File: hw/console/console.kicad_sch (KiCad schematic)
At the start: 1 part, among them U1 F133-A

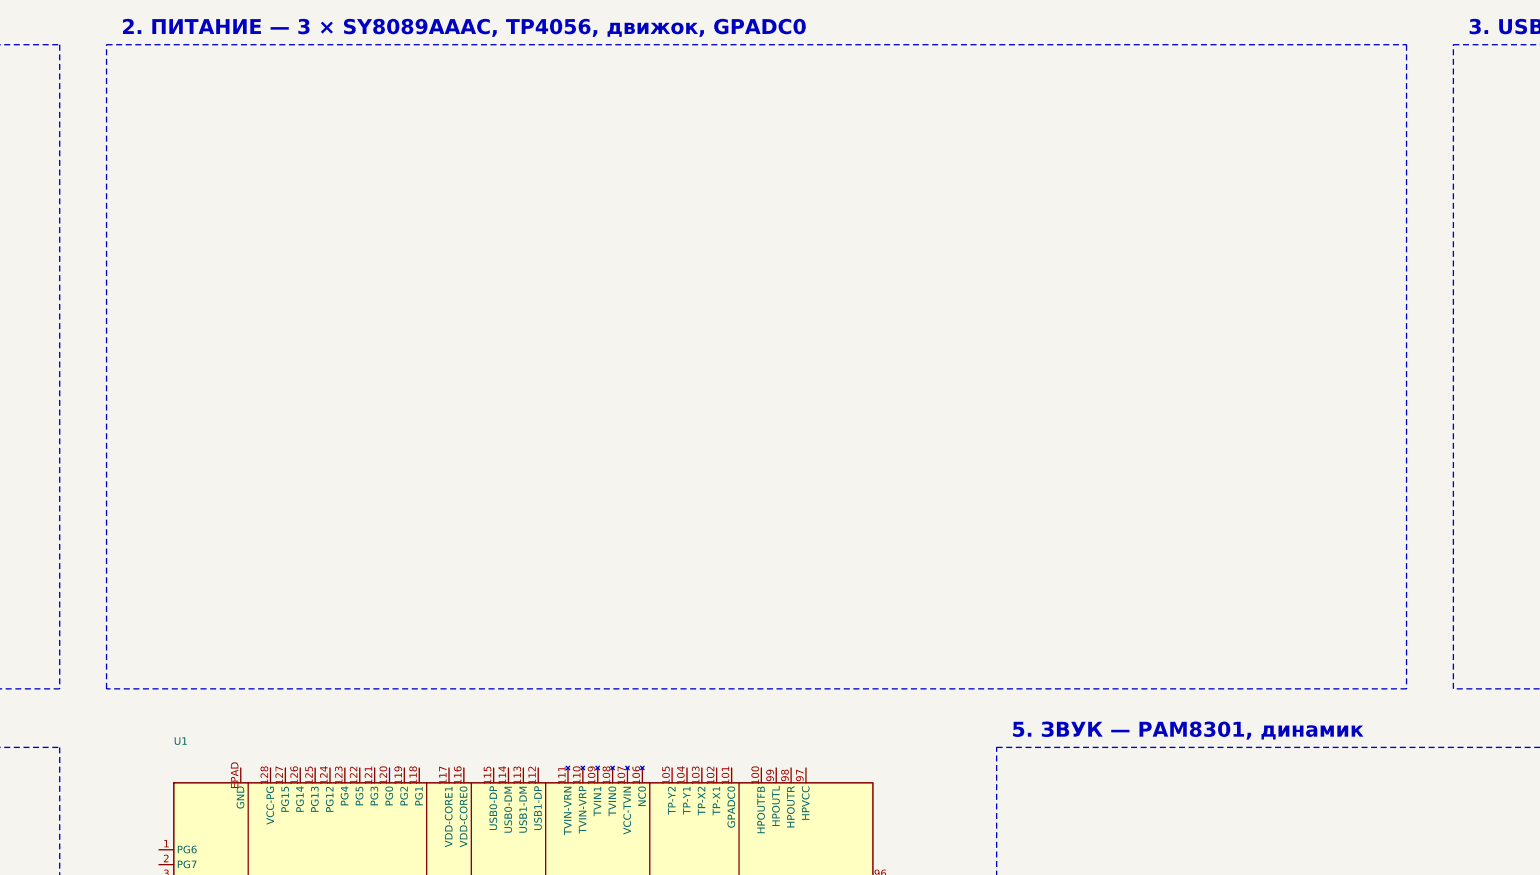
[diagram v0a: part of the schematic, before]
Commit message: hw: блок 2 «Питание» нарисован в KiCad
Три бака SY8089AAAC (3.3 / 1.8 / 0.9 В) с делителями MangoPi, RC-секвенсор
от движка, TP4056 с индикаторами, делитель банки на GPADC0, перемычки и
контрольные точки. Разъём банки — как J3 на плате v1.

Схема генерируется tools/block02_power.py: скрипт идемпотентный, у каждой
детали в поле «Источник» лежит раздел blocks/02-power.md — правило «ни одного
номинала без ссылки на источник» проверяется прямо по схеме.

Сверено по первоисточникам: распиновка SY8089 и TP4056 — по даташитам,
номиналы делителей и порядок старта рельс — по MangoPi. Netlist выгружен и
разобран по цепям: обратные связи, узел PWR_EN, VSYS, VBUS, GND и GPADC0
собираются целиком. ERC — 160 нарушений, все на невыведенных пока выводах
F133, кроме VBUS: его источник появится в блоке 3 вместе с разъёмом USB-C.

Отдельно: KiCad 9.0.9 не применяет (hide yes) в (effects), если рядом нет
(justify), — из-за этого служебные ссылки #PWR/#FLG печатались в PDF.

Co-Authored-By: Claude Opus 5 <noreply@anthropic.com>
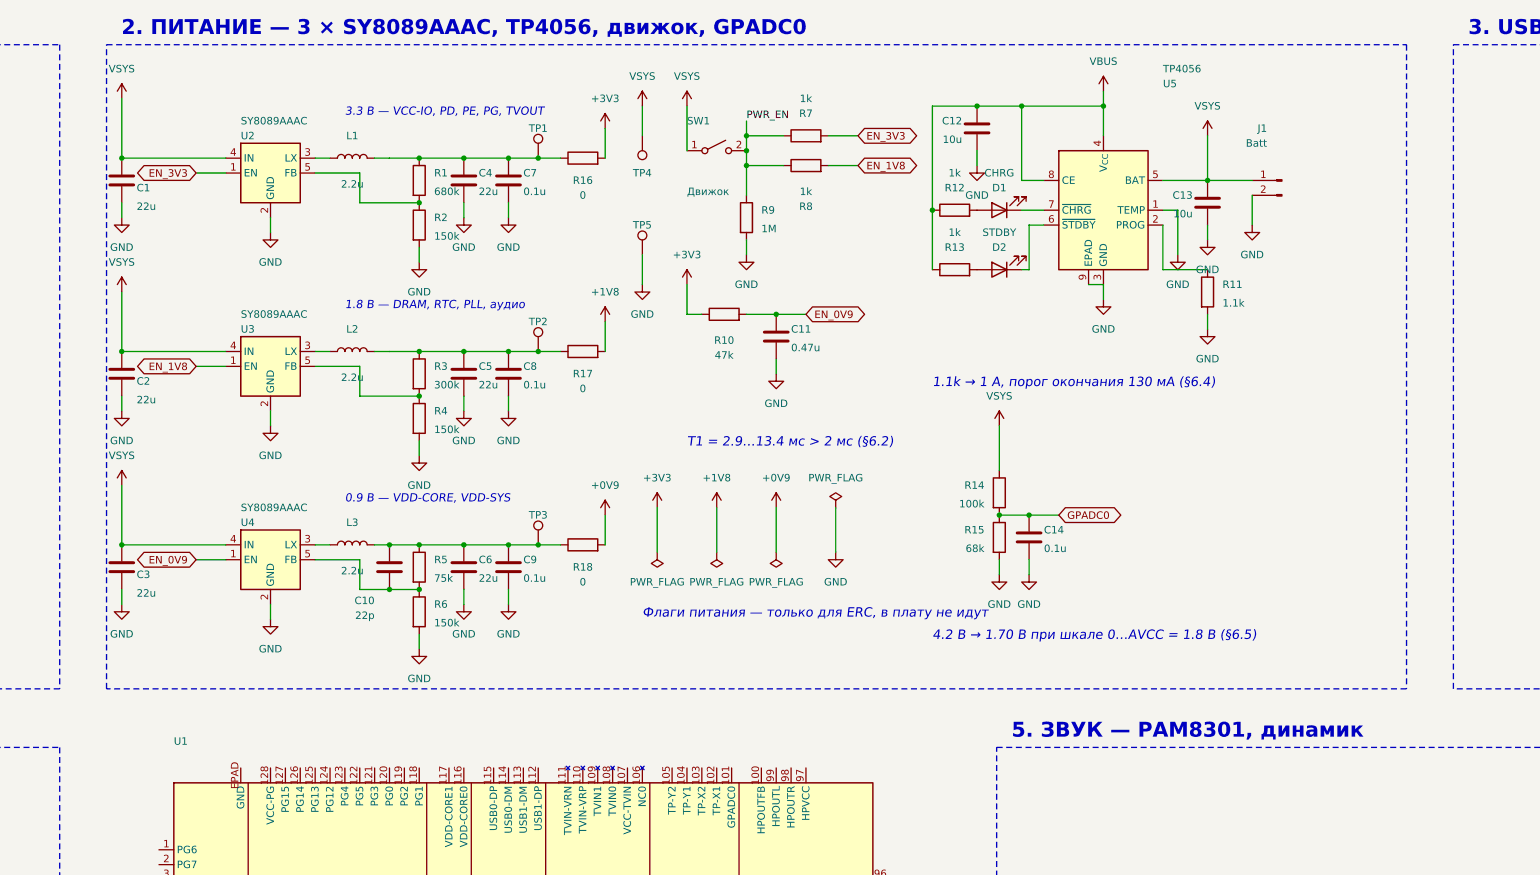
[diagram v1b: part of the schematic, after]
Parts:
- added C1, C2, C3, C4, C5, C6: 22u, Capacitor_SMD:C_0805_2012Metric_Pad1.18x1.45mm_HandSolder, symbol Device:C
- added C10: 22p, Capacitor_SMD:C_0805_2012Metric_Pad1.18x1.45mm_HandSolder, symbol Device:C
- added C11: 0.47u, Capacitor_SMD:C_0805_2012Metric_Pad1.18x1.45mm_HandSolder, symbol Device:C
- added C12, C13: 10u, Capacitor_SMD:C_0805_2012Metric_Pad1.18x1.45mm_HandSolder, symbol Device:C
- added C14, C7, C8, C9: 0.1u, Capacitor_SMD:C_0805_2012Metric_Pad1.18x1.45mm_HandSolder, symbol Device:C
- added D1: CHRG, LED_SMD:LED_0805_2012Metric_Pad1.15x1.40mm_HandSolder, symbol Device:LED
- added D2: STDBY, LED_SMD:LED_0805_2012Metric_Pad1.15x1.40mm_HandSolder, symbol Device:LED
- added J1: Batt, Connector_PinHeader_2.54mm:PinHeader_1x02_P2.54mm_Vertical, symbol Connector:Conn_01x02_Pin
- added L1, L2, L3: 2.2u, symbol Device:L
- added R1: 680k, Resistor_SMD:R_0805_2012Metric_Pad1.20x1.40mm_HandSolder, symbol Device:R
- added R10: 47k, Resistor_SMD:R_0805_2012Metric_Pad1.20x1.40mm_HandSolder, symbol Device:R
- added R11: 1.1k, Resistor_SMD:R_0805_2012Metric_Pad1.20x1.40mm_HandSolder, symbol Device:R
- added R12, R13, R7, R8: 1k, Resistor_SMD:R_0805_2012Metric_Pad1.20x1.40mm_HandSolder, symbol Device:R
- added R14: 100k, Resistor_SMD:R_0805_2012Metric_Pad1.20x1.40mm_HandSolder, symbol Device:R
- added R15: 68k, Resistor_SMD:R_0805_2012Metric_Pad1.20x1.40mm_HandSolder, symbol Device:R
- added R16, R17, R18: 0, Resistor_SMD:R_0805_2012Metric_Pad1.20x1.40mm_HandSolder, symbol Device:R
- added R2, R4, R6: 150k, Resistor_SMD:R_0805_2012Metric_Pad1.20x1.40mm_HandSolder, symbol Device:R
- added R3: 300k, Resistor_SMD:R_0805_2012Metric_Pad1.20x1.40mm_HandSolder, symbol Device:R
- added R5: 75k, Resistor_SMD:R_0805_2012Metric_Pad1.20x1.40mm_HandSolder, symbol Device:R
- added R9: 1M, Resistor_SMD:R_0805_2012Metric_Pad1.20x1.40mm_HandSolder, symbol Device:R
- added SW1: Движок, symbol Switch:SW_SPST
- added TP1: +3V3, TestPoint:TestPoint_Pad_D1.5mm, symbol Connector:TestPoint
- added TP2: +1V8, TestPoint:TestPoint_Pad_D1.5mm, symbol Connector:TestPoint
- added TP3: +0V9, TestPoint:TestPoint_Pad_D1.5mm, symbol Connector:TestPoint
- added TP4: VSYS, TestPoint:TestPoint_Pad_D1.5mm, symbol Connector:TestPoint
- added TP5: GND, TestPoint:TestPoint_Pad_D1.5mm, symbol Connector:TestPoint
- added U2, U3, U4: SY8089AAAC, Package_TO_SOT_SMD:SOT-23-5_HandSoldering, symbol parts:SY8089AAAC
- added U5: TP4056, Package_SO:SOIC-8-1EP_3.9x4.9mm_P1.27mm_EP2.41x3.3mm_ThermalVias, symbol Battery_Management:TP4056-42-ESOP8
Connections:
- new net: D1.1 (K), U5.7 (~{CHRG})
- new net: D1.2 (A), R12.2
- new net: C10.2, R5.2, R6.1, U4.5 (FB)
- new net: C5.1, C8.1, L2.2, R17.1, R3.1, TP2.1
- new net: L2.1, U3.3 (LX)
- new net: R11.1, U5.2 (PROG)
- new net: C4.1, C7.1, L1.2, R1.1, R16.1, TP1.1
- new net: L3.1, U4.3 (LX)
- new net: C10.1, C6.1, C9.1, L3.2, R18.1, R5.1, TP3.1
- new net: R3.2, R4.1, U3.5 (FB)
- new net: D2.2 (A), R13.2
- new net: D2.1 (K), U5.6 (~{STDBY})
- new net: R1.2, R2.1, U2.5 (FB)
- new net: L1.1, U2.3 (LX)
- new net +0V9: R18.2
- new net +1V8: R17.2
- new net +3V3: R10.1, R16.2
- new net EN_0V9: C11.1, R10.2, U4.1 (EN)
- new net EN_1V8: R8.2, U3.1 (EN)
- new net EN_3V3: R7.2, U2.1 (EN)
- new net GND: C1.2, C11.2, C12.2, C13.2, C14.2, C2.2, C3.2, C4.2, C5.2, C6.2, C7.2, C8.2, C9.2, J1.2 (Pin_2), R11.2, R15.2, R2.2, R4.2, R6.2, R9.2, TP5.1, U2.2 (GND), U3.2 (GND), U4.2 (GND), U5.1 (TEMP), U5.3 (GND), U5.9 (EPAD)
- new net GPADC0: C14.1, R14.2, R15.1
- new net PWR_EN: R7.1, R8.1, R9.1, SW1.2 (B)
- new net VBUS: C12.1, R12.1, R13.1, U5.4 (V_{CC}), U5.8 (CE)
- new net VSYS: C1.1, C13.1, C2.1, C3.1, J1.1 (Pin_1), R14.1, SW1.1 (A), TP4.1, U2.4 (IN), U3.4 (IN), U4.4 (IN), U5.5 (BAT)
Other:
- note added: "0.9 В — VDD-CORE, VDD-SYS"
- note added: "1.1k → 1 А, порог окончания 130 мА (§6.4)"
- note added: "1.8 В — DRAM, RTC, PLL, аудио"
- note added: "3.3 В — VCC-IO, PD, PE, PG, TVOUT"
- note added: "4.2 В → 1.70 В при шкале 0…AVCC = 1.8 В (§6.5)"
- note added: "T1 = 2.9…13.4 мс > 2 мс (§6.2)"
- note added: "Флаги питания — только для ERC, в плату не идут"

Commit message: hw: проверка блока 2 — восемь находок, из них две существенные
Существенное:

- корпуса пассива не проставлялись вообще: константы FP_* в генераторе были
  объявлены и ни разу не использованы, весь пассив уходил в netlist с пустым
  Footprint. Теперь 0805 HandSolder; без корпуса осознанно остались дроссели
  и движок — сами детали не выбраны, и пустое поле будет напоминать;
- 02-power.md §2.3 в итоговой строке утверждал «все 1.8 В раньше 3.3 В», что
  прямо противоречит §5 и §6.2. Figure 5-28 даташит называет примером, а не
  требованием; требований про порядок в тексте всего два. Формулировка
  исправлена, иначе на этом можно было переделать секвенсор впустую.

Закупка и документы:

- CHIPS.md: добавлен пассив блока 2 (состав взят из схемы, из закромов вычтено
  по BOARD-draft.md §8) и движок в список невыбранного;
- CHIPS.md §10: «выключенная приставка нагрузки не создаёт вообще» — после
  делителя батареи неверно, там 25 мкА. Вывод про заряд не меняется: это в
  5000 раз меньше порога окончания;
- README: статус блока, parts.kicad_sym, вывод 107 стал power_in, актуальное
  число ERC, раздел про то, как рисуются блоки;
- TZ.md: у индукторов закрыт параметр, осталась только конкретная деталь;
- 02-power.md: ступень 0.9 В берётся с рельсы после перемычки, контрольные
  точки стоят до неё, RC при выключении работает наоборот (§5.13.2 это
  разрешает).

Мелочи в генераторе: два провода нулевой длины (выводы светодиода и резистора
совпадают), поле «Источник» приведено к единому виду, у светодиодов в номинале
цвет.

Netlist поэлементно сверен с эталоном предыдущего коммита — не изменился.
ERC — те же 160.

Co-Authored-By: Claude Opus 5 <noreply@anthropic.com>
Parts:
- C1, C2, C3, C4, C5, C6: Источник §2.4 -> 02-power.md §2.4
- C10: Источник §2.4, §7.5 -> 02-power.md §2.4, §7.5
- C12, C13, R11, R12, R13: Источник §2.5 -> 02-power.md §2.5
- C7, C8, C9: Источник §3, §4 -> 02-power.md §3, §4
- D1: value CHRG -> красный; Источник §2.5 -> 02-power.md §2.5
- D2: value STDBY -> зелёный; Источник §2.5 -> 02-power.md §2.5
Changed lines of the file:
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@@
 			)
 		)
-		(property "Источник" "§2.4"
+		(property "Источник" "02-power.md §2.4"
 			(at 228.6 43.18 0)
 			(effects
@@
 			)
 		)
-		(property "Источник" "§2.4"
+		(property "Источник" "02-power.md §2.4"
 			(at 287.02 43.18 0)
 			(effects
@@
 			)
 		)
-		(property "Источник" "§3, §4"
+		(property "Источник" "02-power.md §3, §4"
 			(at 294.64 43.18 0)
 			(effects
@@
 			)
 		)
-		(property "Источник" "§2.4"
+		(property "Источник" "02-power.md §2.4"
 			(at 228.6 76.2 0)
 			(effects
@@
 			)
 		)
-		(property "Источник" "§2.4"
+		(property "Источник" "02-power.md §2.4"
 			(at 287.02 76.2 0)
 			(effects
@@
 			)
 		)
-		(property "Источник" "§3, §4"
+		(property "Источник" "02-power.md §3, §4"
 			(at 294.64 76.2 0)
 			(effects
@@
 			)
 		)
-		(property "Источник" "§2.4"
+		(property "Источник" "02-power.md §2.4"
 			(at 228.6 109.22 0)
 			(effects
@@
 			)
 		)
-		(property "Источник" "§2.4"
+		(property "Источник" "02-power.md §2.4"
 			(at 287.02 109.22 0)
 			(effects
@@
 			)
 		)
-		(property "Источник" "§3, §4"
+		(property "Источник" "02-power.md §3, §4"
 			(at 294.64 109.22 0)
 			(effects
@@
 			)
 		)
-		(property "Источник" "§2.4, §7.5"
+		(property "Источник" "02-power.md §2.4, §7.5"
 			(at 274.32 109.22 0)
 			(effects
@@
 			)
 		)
-		(property "Источник" "§2.5"
+		(property "Источник" "02-power.md §2.5"
 			(at 374.65 34.29 0)
 			(effects
@@
 			)
 		)
-		(property "Value" "CHRG"
+		(property "Value" "красный"
 			(at 378.46 41.91 0)
 			(effects
@@
 			)
 		)
-		(property "Источник" "§2.5"
+		(property "Источник" "02-power.md §2.5"
 			(at 378.46 48.26 0)
 			(effects
@@
 			)
 		)
-		(property "Источник" "§2.5"
+		(property "Источник" "02-power.md §2.5"
 			(at 370.84 48.26 0)
 			(effects
@@
 		(stroke (width 0) (type default))
 	)
-	(wire
-		(pts (xy 374.65 48.26) (xy 374.65 48.26))
-		(stroke (width 0) (type default))
-	)
 	(symbol
 		(lib_id "Device:LED")
@@
 			)
 		)
-		(property "Value" "STDBY"
+		(property "Value" "зелёный"
 			(at 378.46 52.07 0)
 			(effects
@@
 			)
 		)
-		(property "Источник" "§2.5"
+		(property "Источник" "02-power.md §2.5"
 			(at 378.46 58.42 0)
 			(effects
@@
 			)
 		)
-		(property "Источник" "§2.5"
+		(property "Источник" "02-power.md §2.5"
 			(at 370.84 58.42 0)
 			(effects
@@
 		(stroke (width 0) (type default))
 	)
-	(wire
-		(pts (xy 374.65 58.42) (xy 374.65 58.42))
-		(stroke (width 0) (type default))
-	)
 	(junction
 		(at 367.03 48.26)
@@
 			)
 		)
-		(property "Источник" "§2.5"
+		(property "Источник" "02-power.md §2.5"
 			(at 414.02 46.99 0)
 			(effects
@@
 			)
 		)
-		(property "Источник" "§2.5"
+		(property "Источник" "02-power.md §2.5"
 			(at 414.02 62.23 0)
 			(effects

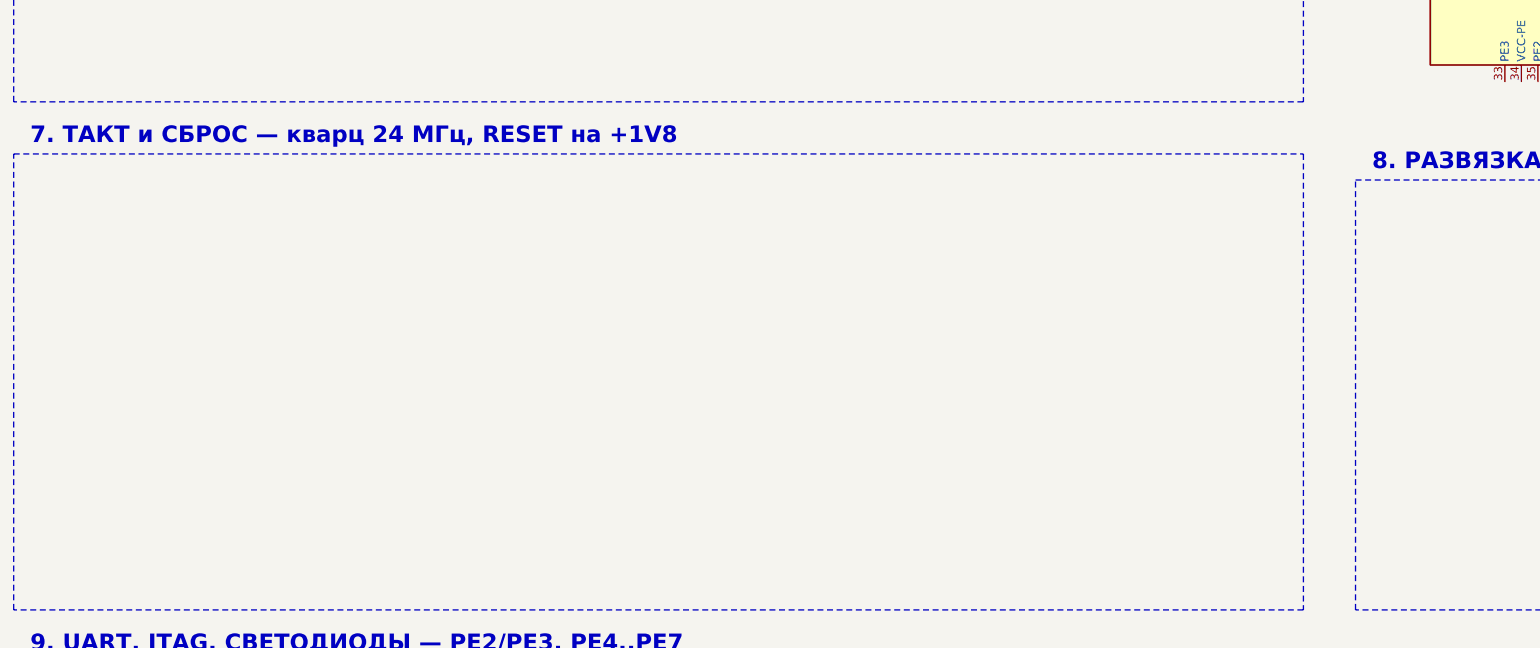
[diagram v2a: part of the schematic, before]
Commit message: hw: блок 7 «Такт и сброс» нарисован, машинерия генераторов вынесена в модуль
Кварц 24 МГц с нагрузочными 22 пФ, кварц 32.768 кГц с такими же, цепь RESET:
подтяжка 10k на +1V8, 0.1 мкФ и кнопка PTS645. Резистор смещения 10M у кварца
32 кГц на схеме есть, но не монтируется — место на случай, если генератор не
заведётся.

Что выяснилось при сборе документа:

- подтяжку RESET платы делают по-разному: MangoPi на 1.8 В (LDOA-OUT, 10K),
  Xassette на 3.3 В (100k). Table 4-2 относит вывод 27 к домену VCC-RTC, а
  «pull up 3.3 V» в Table 5-12 стоит в условиях измерения, а не в требованиях.
  Берём 1.8 В, как MangoPi;
- требование §5.13.1 держать RESET низким 64 мс закрывает сам чип: Table 5-12
  даёт внутренний сброс ровно на 64 мс, и обе платы внешней задержки не делают.
  Соответственно поправлена оценка в 02-power.md §6.6;
- номиналов нагрузочных ёмкостей даташит не даёт вовсе, отсылает к схеме,
  которой у нас нет. Взяты с MangoPi и проверены его же формулой:
  22/2 + 6.5 = 17.5 при CL 18 пФ и 22/2 + 1.1 = 12.1 при CL 12.5 пФ.

Кварц 32.768 кГц и корпус 3225 для 24 МГц — решения Андрея; даташит §5.9.2
разрешает обойтись внутренним RC, но тогда точность RTC зависела бы от
прошивки, а место после разводки не вернуть.

Машинерия генераторов вынесена в tools/kicadsch.py: иначе исправленные грабли
KiCad пришлось бы чинить в каждом из девяти блоков заново. Проверено, что
блок 2 после переезда даёт побайтово ту же схему.

Найдено прогоном: блок 7 выдал ссылки #PWR000..#PWR007, уже занятые блоком 2, —
нумерация шла от нуля внутри блока. Теперь номер блока входит в ссылку.

Netlist: DXIN, DXOUT, X32KIN, X32KOUT и RESET собираются целиком, +1V8 впервые
получила потребителя. ERC — те же 160, все на невыведенных выводах F133, кроме
VBUS из блока 3.

Co-Authored-By: Claude Opus 5 <noreply@anthropic.com>
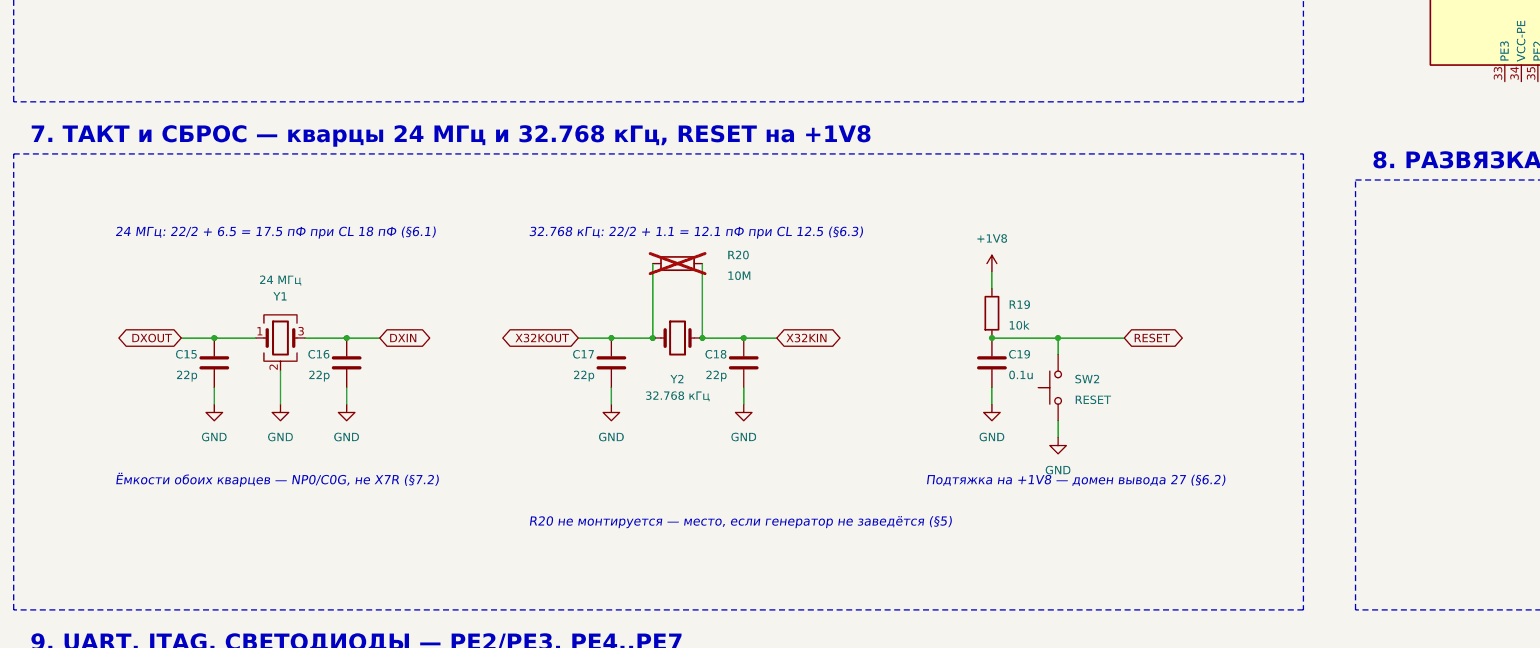
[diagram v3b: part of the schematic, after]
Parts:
- added C15, C16, C17, C18: 22p, Capacitor_SMD:C_0805_2012Metric_Pad1.18x1.45mm_HandSolder, symbol Device:C
- added C19: 0.1u, Capacitor_SMD:C_0805_2012Metric_Pad1.18x1.45mm_HandSolder, symbol Device:C
- added R19: 10k, Resistor_SMD:R_0805_2012Metric_Pad1.20x1.40mm_HandSolder, symbol Device:R
- added R20: 10M, Resistor_SMD:R_0805_2012Metric_Pad1.20x1.40mm_HandSolder, symbol Device:R
- added SW2: RESET, Button_Switch_SMD:SW_SPST_PTS645Sx43SMTR92, symbol Switch:SW_Push
- added Y1: 24 МГц, Crystal:Crystal_SMD_3225-4Pin_3.2x2.5mm_HandSoldering, symbol Device:Crystal_GND24
- added Y2: 32.768 кГц, Crystal:Crystal_SMD_3215-2Pin_3.2x1.5mm, symbol Device:Crystal
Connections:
- net +1V8: now also R19.1
- net GND: now also C15.2, C16.2, C17.2, C18.2, C19.2, SW2.1, Y1.2 (G), Y1.4 (G)
- new net DXIN: C16.1, Y1.3
- new net DXOUT: C15.1, Y1.1
- new net RESET: C19.1, R19.2, SW2.2
- new net X32KIN: C18.1, R20.2, Y2.2
- new net X32KOUT: C17.1, R20.1, Y2.1
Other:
- note added: "24 МГц: 22/2 + 6.5 = 17.5 пФ при CL 18 пФ (§6.1)"
- note added: "32.768 кГц: 22/2 + 1.1 = 12.1 пФ при CL 12.5 (§6.3)"
- note added: "7. ТАКТ и СБРОС — кварцы 24 МГц и 32.768 кГц, RESET на +1V8"
- note added: "R20 не монтируется — место, если генератор не заведётся (§5)"
- note added: "Ёмкости обоих кварцев — NP0/C0G, не X7R (§7.2)"
- note added: "Подтяжка на +1V8 — домен вывода 27 (§6.2)"
- note removed: "7. ТАКТ и СБРОС — кварц 24 МГц, RESET на +1V8"
